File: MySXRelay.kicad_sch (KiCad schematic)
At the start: 44 parts, among them J3 Relay, Q2 BSS84A, U1 AP2204RA-5.0, U2 BL0942, U3 BP2525X, U4 Si8642BB-B-IS1, U5 AP2127N-3.3, U9 ST485E, X1 RS485, X2 Mains

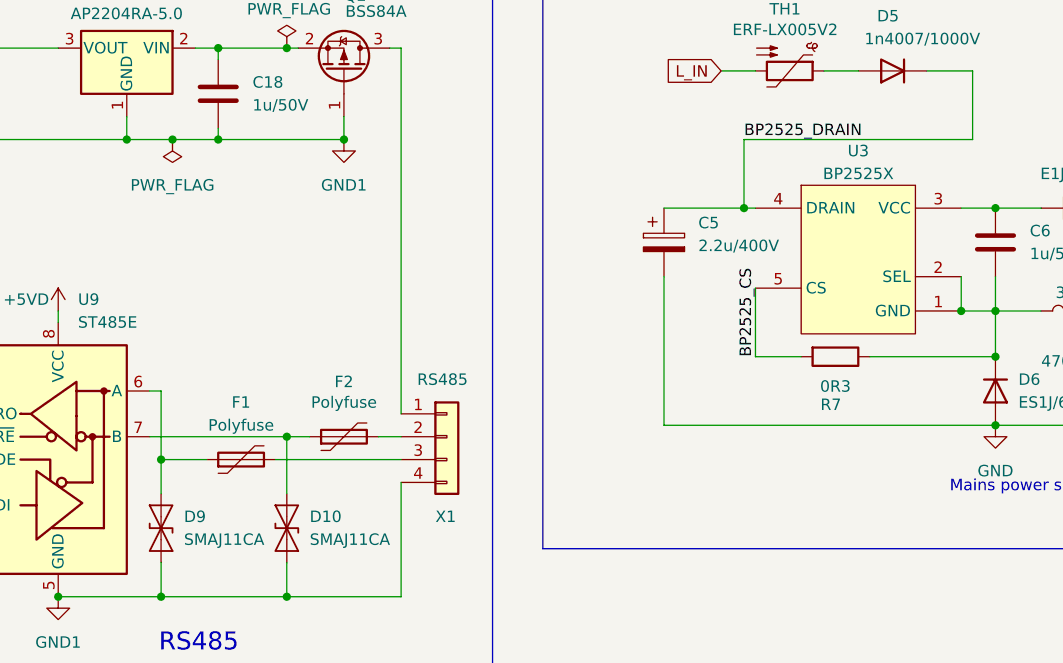
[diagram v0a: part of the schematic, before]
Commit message: fix part names and datasheet links
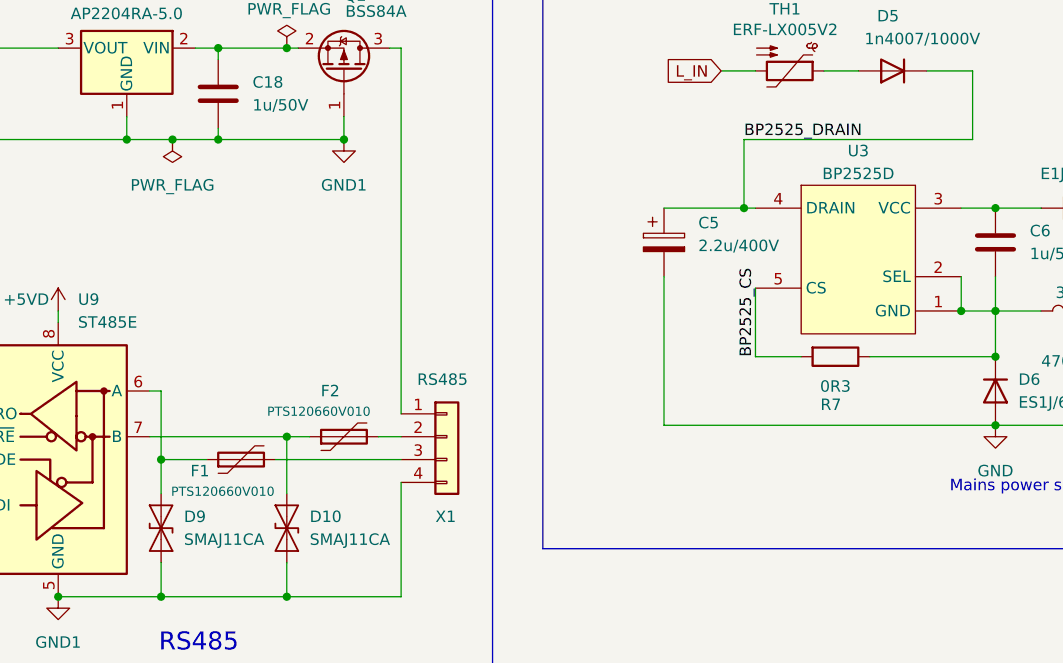
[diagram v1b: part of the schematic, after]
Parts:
- F1, F2: value Polyfuse -> PTS120660V010
- U3: value BP2525X -> BP2525D
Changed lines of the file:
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@@
 	(label "BP2525_CS"
 		(at 175.26 143.51 90)
-		(fields_autoplaced yes)
 		(effects
 			(font
@@
 	(label "BP2525_DRAIN"
 		(at 173.99 119.38 0)
-		(fields_autoplaced yes)
 		(effects
 			(font
@@
 			)
 		)
-		(property "Value" "BP2525X"
+		(property "Value" "BP2525D"
 			(at 186.69 123.19 0)
 			(effects
@@
 		(on_board yes)
 		(dnp no)
-		(fields_autoplaced yes)
 		(property "Reference" "F1"
-			(at 118.11 148.59 90)
-			(effects
-				(font
-					(size 1.27 1.27)
-				)
-			)
-		)
-		(property "Value" "Polyfuse"
-			(at 118.11 151.13 90)
-			(effects
-				(font
-					(size 1.27 1.27)
+			(at 113.538 156.21 90)
+			(effects
+				(font
+					(size 1.27 1.27)
+				)
+			)
+		)
+		(property "Value" "PTS120660V010"
+			(at 116.078 158.496 90)
+			(effects
+				(font
+					(size 1.016 1.016)
 				)
 			)
@@
 		(dnp no)
 		(property "Reference" "F2"
-			(at 129.54 146.304 90)
-			(effects
-				(font
-					(size 1.27 1.27)
-				)
-			)
-		)
-		(property "Value" "Polyfuse"
-			(at 129.54 148.59 90)
-			(effects
-				(font
-					(size 1.27 1.27)
-				)
-			)
+			(at 128.016 147.32 90)
+			(effects
+				(font
+					(size 1.27 1.27)
+				)
+			)
+		)
+		(property "Value" "PTS120660V010"
+			(at 126.746 149.606 90)
+			(effects
+				(font
+					(size 1.016 1.016)
+				)
+			)

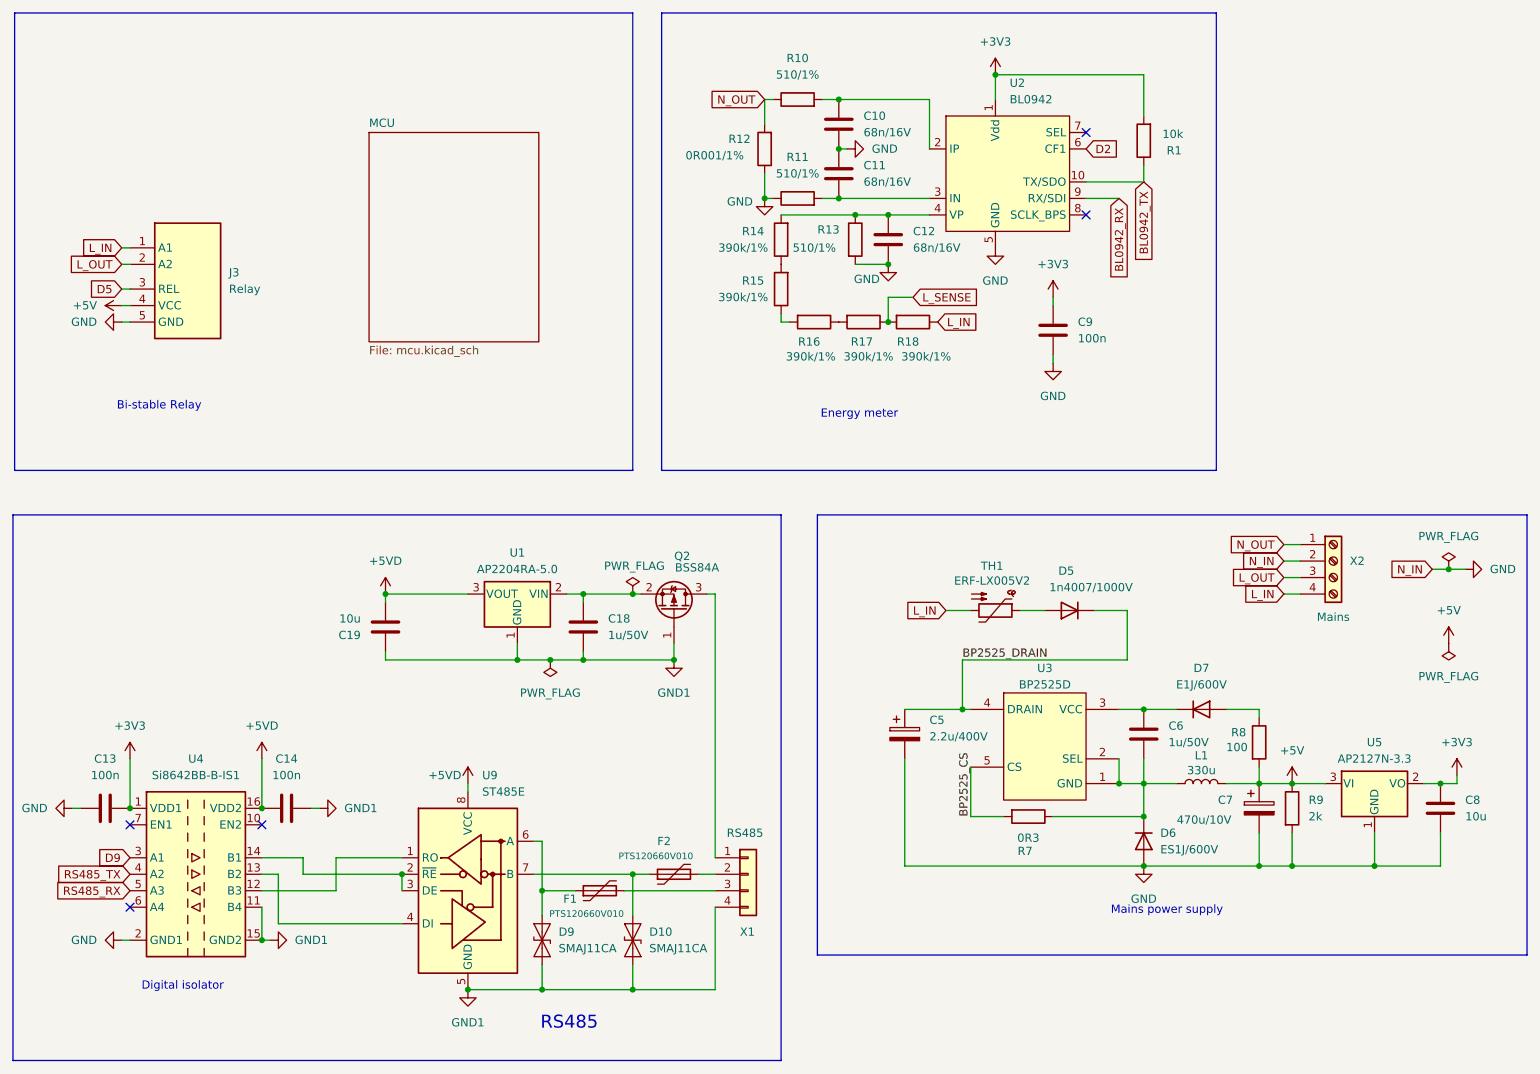
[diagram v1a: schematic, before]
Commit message: replace RS485 low voltage side with single isolated transciever chip CA-IS3092W
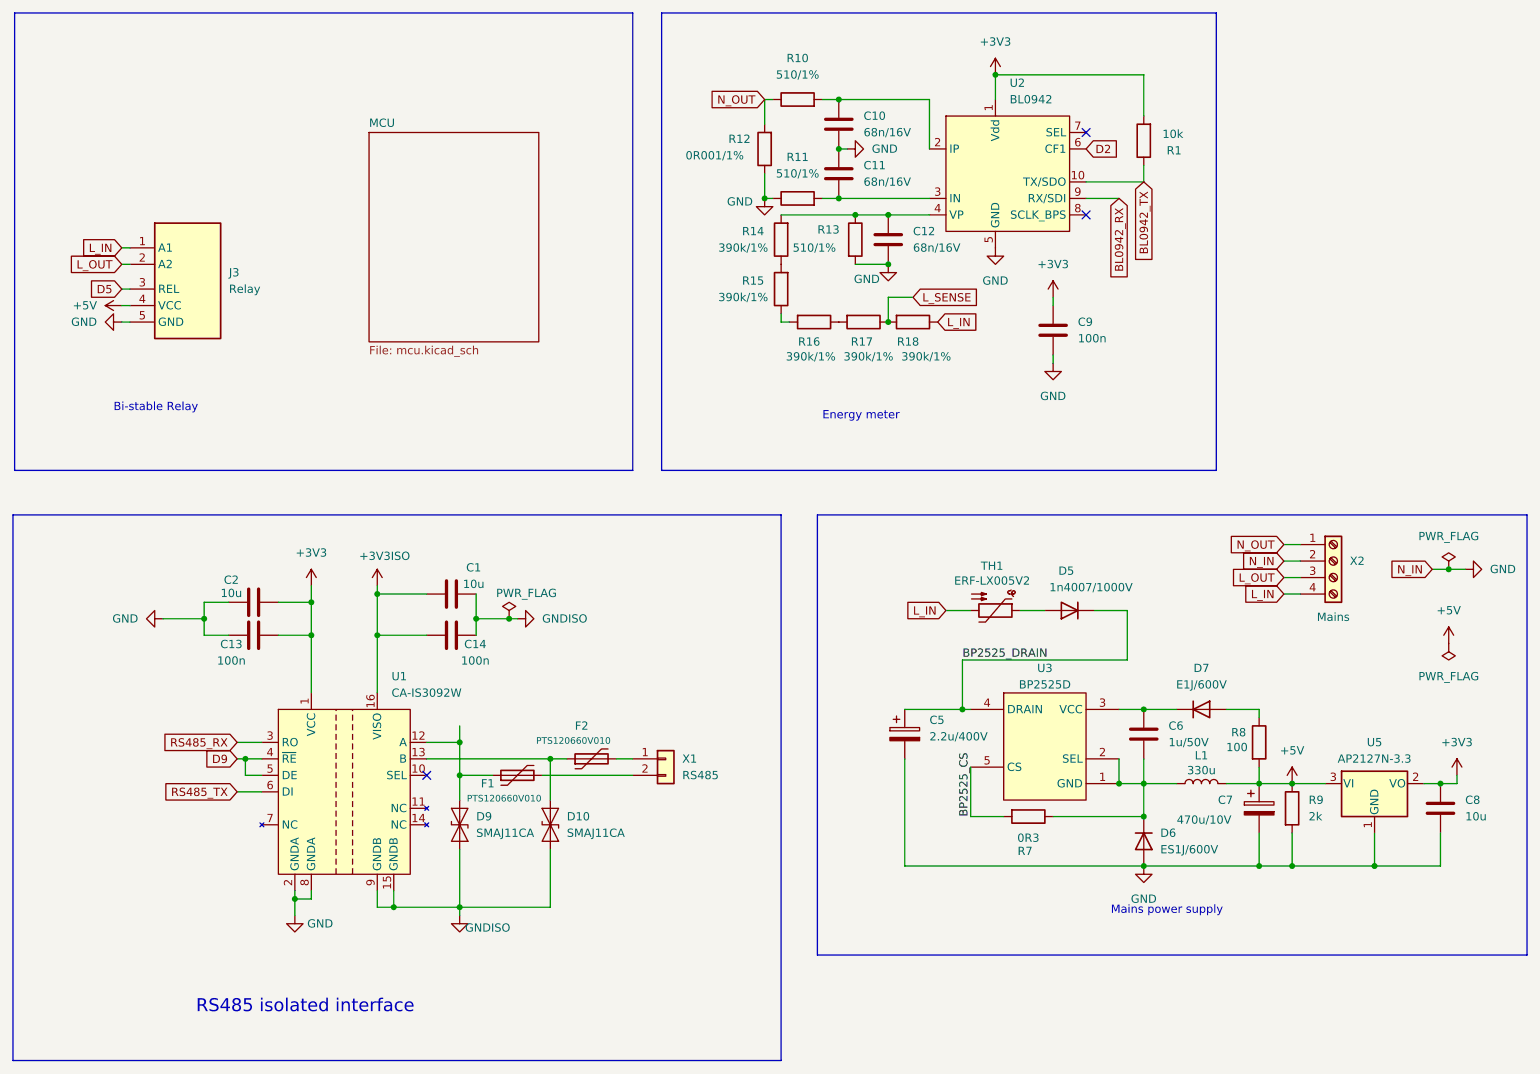
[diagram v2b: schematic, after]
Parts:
- removed C18: 1u/50V, Capacitor_SMD:C_0603_1608Metric, symbol Device:C
- removed C19: 10u, Capacitor_SMD:C_0603_1608Metric, symbol Device:C
- removed Q2: BSS84A, Package_TO_SOT_SMD:SOT-23, symbol Device:Q_PMOS_GSD
- removed U1: AP2204RA-5.0, Package_TO_SOT_SMD:SOT-89-3, symbol Regulator_Linear:AP2204RA-5.0
- removed U4: Si8642BB-B-IS1, Package_SO:SOIC-16_3.9x9.9mm_P1.27mm, symbol Isolator:Si8642BB-B-IS1
- removed U9: ST485E, Package_SO:SOIC-8_3.9x4.9mm_P1.27mm, symbol Interface_UART:ST485E
- removed X1: RS485, MySXRelay:JST-XH_S_4P-2.54MM-PIN1-RIGHT, symbol Connector_Generic:Conn_01x04
- added C1, C2: 10u, Capacitor_SMD:C_0603_1608Metric, symbol Device:C
- added U1: CA-IS3092W, MySXRelay:SOIC-16W_7.5x10.3mm_P1.27mm, symbol MySXRelay:CA-IS3092W
- added X1: RS485, MySXRelay:JST-XH_S_2P-2.54MM, symbol Connector_Generic:Conn_01x02
- D10, D9: footprint Diode_SMD:D_SMA -> MySXRelay:D_SMA
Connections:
- net +3V3: now also C2.2, U1.1 (VCC)
- net D9: now also U1.4 (~{RE}), U1.5 (DE)
- net GND: now also C2.1, U1.2 (GNDA), U1.8 (GNDA)
- net RS485_RX: now also U1.3 (RO)
- net RS485_TX: now also U1.6 (DI)
- net at D9.2 (A2), F1.1: now also U1.12 (A)
- net at F1.2: now also X1.2 (Pin_2)
- net at D10.2 (A2), F2.1: now also U1.13 (B)
- net at F2.2: now also X1.1 (Pin_1)
- net +5VD renamed +3V3ISO
- net +3V3ISO: now also C1.1, U1.16 (VISO)
- net GND1 renamed GNDISO
- net GNDISO: now also C1.2, U1.15 (GNDB), U1.9 (GNDB)
- no-connect marks 5 -> 3
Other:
- note added: "RS485 isolated interface"
- note removed: "Digital isolator"
- note removed: "RS485"
- moved on the sheet: C13, C14, D10, D9, F1, F2

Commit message: rework for proper clearence distances
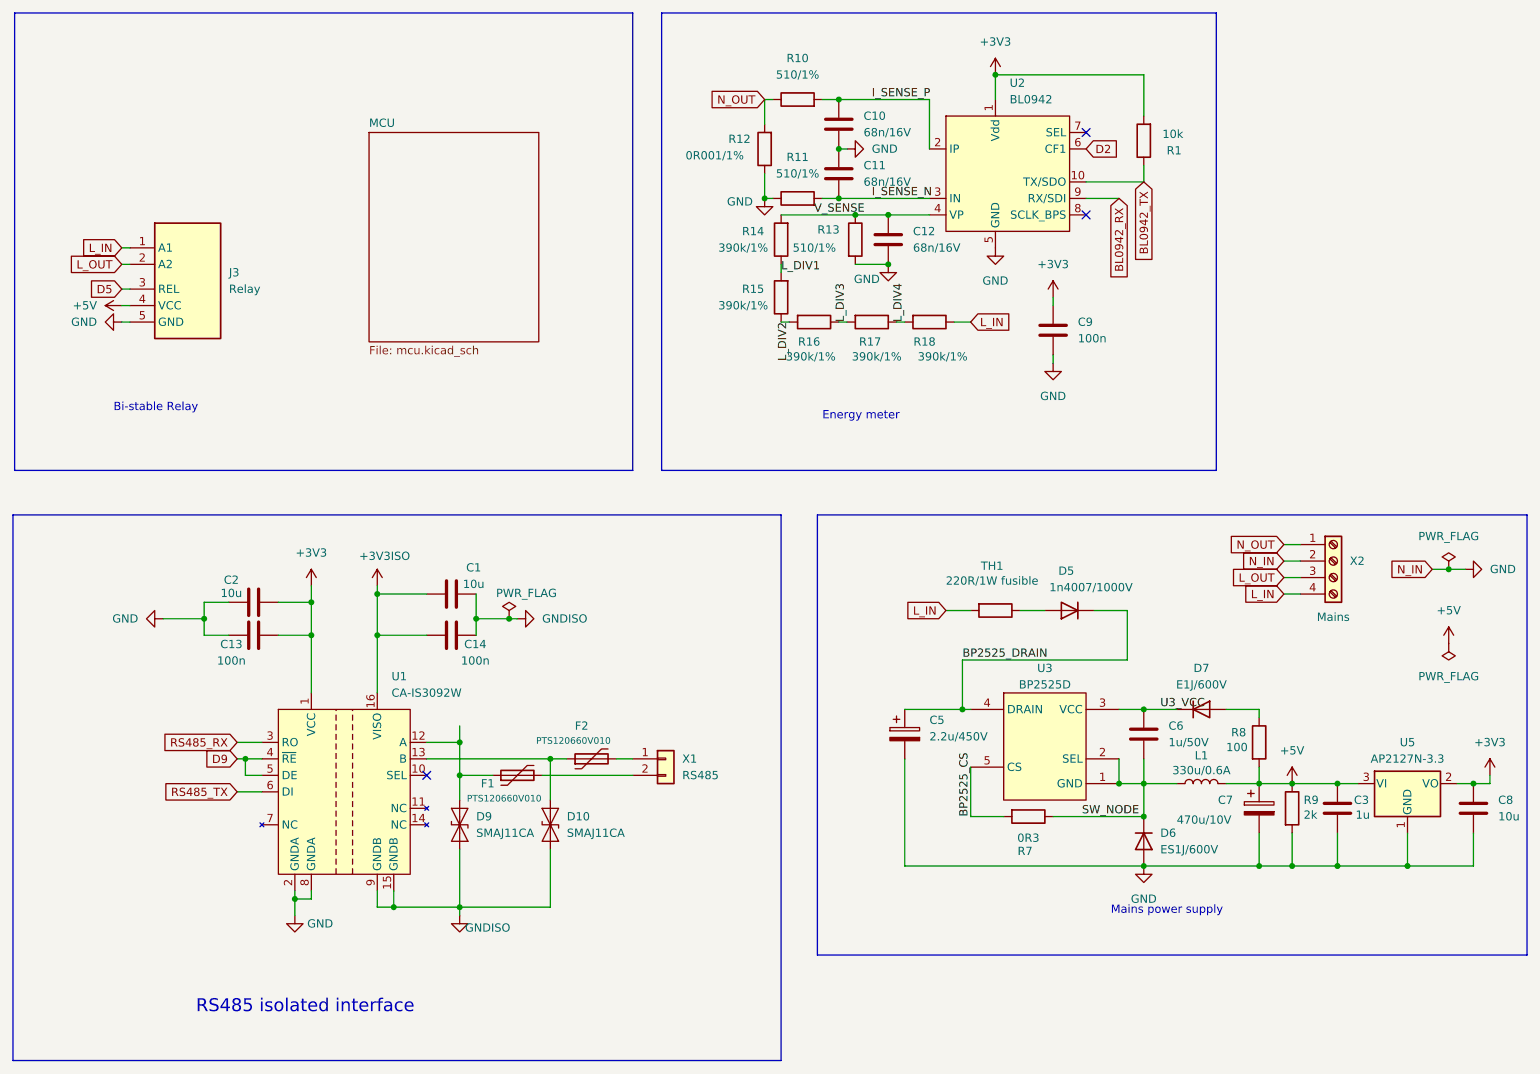
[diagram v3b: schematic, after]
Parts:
- added C3: 1u, Capacitor_SMD:C_0603_1608Metric, symbol Device:C
- C5: value 2.2u/400V -> 2.2u/450V
- L1: value 330u -> 330u/0.6A; footprint Inductor_THT:L_Radial_D7.0mm_P3.00mm -> MySXRelay:L_Radial_D7.5mm_P3.00mm_Ferrocore_COIL0608
- TH1: value ERF-LX005V2 -> 220R/1W fusible; footprint Fuse:Fuse_Bourns_MF-RG300 -> Resistor_THT:R_Axial_DIN0207_L6.3mm_D2.5mm_P5.08mm_Vertical; symbol Device:Thermistor_PTC -> Device:R
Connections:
- net +5V: now also C3.1
- net GND: now also C3.2
- net U3_VCC: now reaches C6.1, D7.1 (K), U3.3 (VCC)
- net SW_NODE: now reaches C6.2, D6.1 (K), L1.1, R7.1, U3.1 (GND), U3.2 (SEL)
- net V_SENSE: now reaches C12.1, R13.1, R14.2, U2.4 (VP)
- net I_SENSE_P: now reaches C10.1, R10.2, U2.2 (IP)
- net L_DIV1: now reaches R14.1, R15.2
- net I_SENSE_N: now reaches C11.2, R11.2, U2.3 (IN)
- net L_DIV3: now reaches R16.1, R17.2
- net L_DIV2: now reaches R15.1, R16.2
- net L_SENSE renamed L_DIV4
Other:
- moved on the sheet: C8, R15, R17, R18, U5
